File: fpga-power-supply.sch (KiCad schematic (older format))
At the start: 100 parts, among them U14 XC7A100T-FGG484

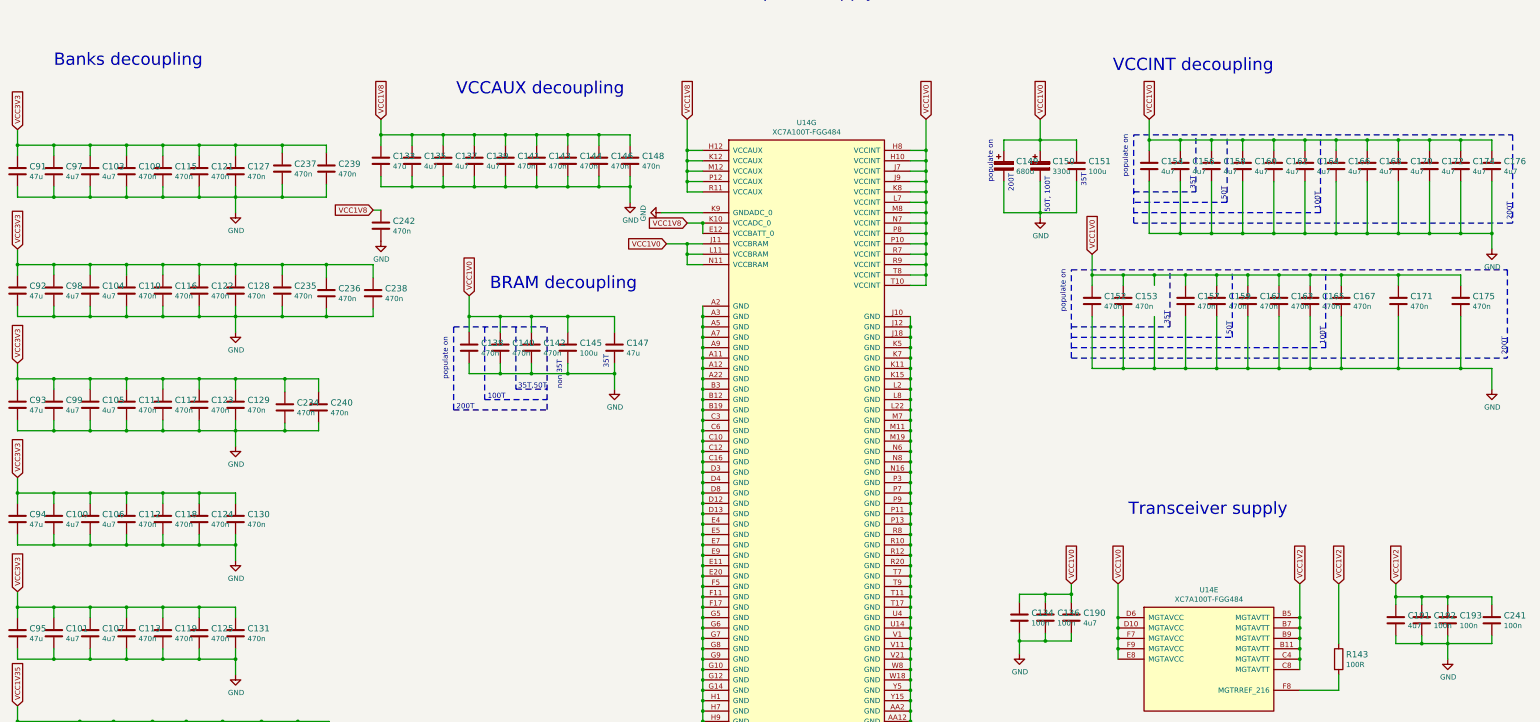
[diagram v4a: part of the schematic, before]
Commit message: Update layout around filtering caps
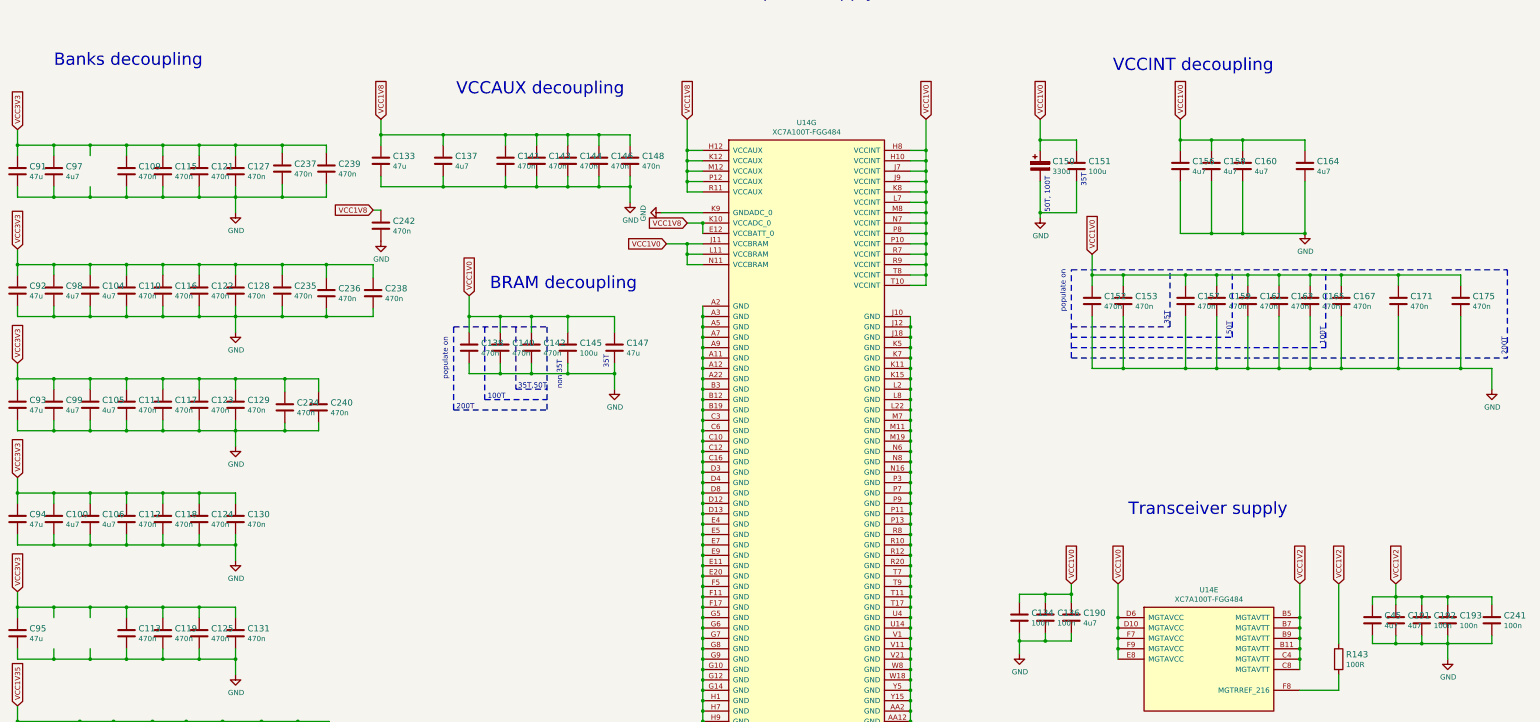
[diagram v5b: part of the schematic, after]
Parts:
- removed C101, C103, C107, C135, C139, C154, C162, C166, C168, C170, C172, C174, C176: C_4u7_0603, artix-dc-scm-footprints:0603-cap, symbol artix-dc-scm:C_4u7_0603
- removed C149: C_680u_KEMET_D, artix-dc-scm-footprints:KEMET_D, symbol artix-dc-scm:C_680u_KEMET_D
- added C45: C_4u7_0603, artix-dc-scm-footprints:0603-cap, symbol artix-dc-scm:C_4u7_0603
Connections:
- net GND: now also C45.2
- net VCC1V2: now also C45.1

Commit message: Generated local libs
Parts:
- C138, C142, C146, C152, C153, C157, C159, C161, C163, C165, C171, C175, C242: footprint antmicro-footprints:0201-res -> artix-dc-scm-footprints:0201-res; symbol antmicroCapacitorsmisc:C_470n_0201 -> artix-dc-scm:C_470n_0201
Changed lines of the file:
@@
 $EndComp
 $Comp
-L antmicroCapacitorsmisc:C_470n_0201 C152
+L artix-dc-scm:C_470n_0201 C152
 U 1 1 603575F3
 P 11500 4350
+AR Path="/603575F3" Ref="C152"  Part="1"
+AR Path="/5FD86C51/603575F3" Ref="C152"  Part="1"
 F 0 "C152" H 11615 4395 60  0000 L CNN
 F 1 "C_470n_0402" H 11500 4200 60  0001 C CNN
-F 2 "antmicro-footprints:0201-res" H 11700 4550 60  0001 L CNN
+F 2 "artix-dc-scm-footprints:0201-res" H 11700 4550 60  0001 L CNN
 F 3 "" H 11500 4350 50  0001 C CNN
 F 4 "TDK" H 11700 4750 60  0001 L CNN "Manufacturer"
@@
 $EndComp
 $Comp
-L antmicroCapacitorsmisc:C_470n_0201 C153
+L artix-dc-scm:C_470n_0201 C153
 U 1 1 60357C64
 P 11800 4350
+AR Path="/60357C64" Ref="C153"  Part="1"
+AR Path="/5FD86C51/60357C64" Ref="C153"  Part="1"
 F 0 "C153" H 11915 4395 60  0000 L CNN
 F 1 "C_470n_0402" H 11800 4200 60  0001 C CNN
-F 2 "antmicro-footprints:0201-res" H 12000 4550 60  0001 L CNN
+F 2 "artix-dc-scm-footprints:0201-res" H 12000 4550 60  0001 L CNN
 F 3 "" H 11800 4350 50  0001 C CNN
 F 4 "TDK" H 12000 4750 60  0001 L CNN "Manufacturer"
@@
 $EndComp
 $Comp
-L antmicroCapacitorsmisc:C_470n_0201 C157
+L artix-dc-scm:C_470n_0201 C157
 U 1 1 603583CC
 P 12400 4350
+AR Path="/603583CC" Ref="C157"  Part="1"
+AR Path="/5FD86C51/603583CC" Ref="C157"  Part="1"
 F 0 "C157" H 12515 4395 60  0000 L CNN
 F 1 "C_470n_0402" H 12400 4200 60  0001 C CNN
-F 2 "antmicro-footprints:0201-res" H 12600 4550 60  0001 L CNN
+F 2 "artix-dc-scm-footprints:0201-res" H 12600 4550 60  0001 L CNN
 F 3 "" H 12400 4350 50  0001 C CNN
 F 4 "TDK" H 12600 4750 60  0001 L CNN "Manufacturer"
@@
 $EndComp
 $Comp
-L antmicroCapacitorsmisc:C_470n_0201 C159
+L artix-dc-scm:C_470n_0201 C159
 U 1 1 6035880F
 P 12700 4350
+AR Path="/6035880F" Ref="C159"  Part="1"
+AR Path="/5FD86C51/6035880F" Ref="C159"  Part="1"
 F 0 "C159" H 12815 4395 60  0000 L CNN
 F 1 "C_470n_0402" H 12700 4200 60  0001 C CNN
-F 2 "antmicro-footprints:0201-res" H 12900 4550 60  0001 L CNN
+F 2 "artix-dc-scm-footprints:0201-res" H 12900 4550 60  0001 L CNN
 F 3 "" H 12700 4350 50  0001 C CNN
 F 4 "TDK" H 12900 4750 60  0001 L CNN "Manufacturer"
@@
 $EndComp
 $Comp
-L antmicroCapacitorsmisc:C_470n_0201 C161
+L artix-dc-scm:C_470n_0201 C161
 U 1 1 60358B3A
 P 13000 4350
+AR Path="/60358B3A" Ref="C161"  Part="1"
+AR Path="/5FD86C51/60358B3A" Ref="C161"  Part="1"
 F 0 "C161" H 13115 4395 60  0000 L CNN
 F 1 "C_470n_0402" H 13000 4200 60  0001 C CNN
-F 2 "antmicro-footprints:0201-res" H 13200 4550 60  0001 L CNN
+F 2 "artix-dc-scm-footprints:0201-res" H 13200 4550 60  0001 L CNN
 F 3 "" H 13000 4350 50  0001 C CNN
 F 4 "TDK" H 13200 4750 60  0001 L CNN "Manufacturer"
@@
 $EndComp
 $Comp
-L antmicroCapacitorsmisc:C_470n_0201 C163
+L artix-dc-scm:C_470n_0201 C163
 U 1 1 60358ED9
 P 13300 4350
+AR Path="/60358ED9" Ref="C163"  Part="1"
+AR Path="/5FD86C51/60358ED9" Ref="C163"  Part="1"
 F 0 "C163" H 13415 4395 60  0000 L CNN
 F 1 "C_470n_0402" H 13300 4200 60  0001 C CNN
-F 2 "antmicro-footprints:0201-res" H 13500 4550 60  0001 L CNN
+F 2 "artix-dc-scm-footprints:0201-res" H 13500 4550 60  0001 L CNN
 F 3 "" H 13300 4350 50  0001 C CNN
 F 4 "TDK" H 13500 4750 60  0001 L CNN "Manufacturer"
@@
 $EndComp
 $Comp
-L antmicroCapacitorsmisc:C_470n_0201 C165
+L artix-dc-scm:C_470n_0201 C165
 U 1 1 60359FF4
 P 13600 4350
+AR Path="/60359FF4" Ref="C165"  Part="1"
+AR Path="/5FD86C51/60359FF4" Ref="C165"  Part="1"
 F 0 "C165" H 13715 4395 60  0000 L CNN
 F 1 "C_470n_0402" H 13600 4200 60  0001 C CNN
-F 2 "antmicro-footprints:0201-res" H 13800 4550 60  0001 L CNN
+F 2 "artix-dc-scm-footprints:0201-res" H 13800 4550 60  0001 L CNN
 F 3 "" H 13600 4350 50  0001 C CNN
 F 4 "TDK" H 13800 4750 60  0001 L CNN "Manufacturer"
@@
 $EndComp
 $Comp
-L antmicroCapacitorsmisc:C_470n_0201 C171
+L artix-dc-scm:C_470n_0201 C171
 U 1 1 6035AD1D
 P 14450 4350
+AR Path="/6035AD1D" Ref="C171"  Part="1"
+AR Path="/5FD86C51/6035AD1D" Ref="C171"  Part="1"
 F 0 "C171" H 14565 4395 60  0000 L CNN
 F 1 "C_470n_0402" H 14450 4200 60  0001 C CNN
-F 2 "antmicro-footprints:0201-res" H 14650 4550 60  0001 L CNN
+F 2 "artix-dc-scm-footprints:0201-res" H 14650 4550 60  0001 L CNN
 F 3 "" H 14450 4350 50  0001 C CNN
 F 4 "TDK" H 14650 4750 60  0001 L CNN "Manufacturer"
@@
 $EndComp
 $Comp
-L antmicroCapacitorsmisc:C_470n_0201 C175
+L artix-dc-scm:C_470n_0201 C175
 U 1 1 6035C6A9
 P 15050 4350
+AR Path="/6035C6A9" Ref="C175"  Part="1"
+AR Path="/5FD86C51/6035C6A9" Ref="C175"  Part="1"
 F 0 "C175" H 15165 4395 60  0000 L CNN
 F 1 "C_470n_0402" H 15050 4200 60  0001 C CNN
-F 2 "antmicro-footprints:0201-res" H 15250 4550 60  0001 L CNN
+F 2 "artix-dc-scm-footprints:0201-res" H 15250 4550 60  0001 L CNN
 F 3 "" H 15050 4350 50  0001 C CNN
 F 4 "TDK" H 15250 4750 60  0001 L CNN "Manufacturer"
@@
 $EndComp
 $Comp
-L antmicroCapacitorsmisc:C_470n_0201 C138
+L artix-dc-scm:C_470n_0201 C138
 U 1 1 603CDFCC
 P 5500 4800
+AR Path="/603CDFCC" Ref="C138"  Part="1"
+AR Path="/5FD86C51/603CDFCC" Ref="C138"  Part="1"
 F 0 "C138" H 5615 4845 60  0000 L CNN
 F 1 "C_470n_0402" H 5500 4650 60  0001 C CNN
-F 2 "antmicro-footprints:0201-res" H 5700 5000 60  0001 L CNN
+F 2 "artix-dc-scm-footprints:0201-res" H 5700 5000 60  0001 L CNN
 F 3 "" H 5500 4800 50  0001 C CNN
 F 4 "TDK" H 5700 5200 60  0001 L CNN "Manufacturer"
@@
 $EndComp
 $Comp
-L antmicroCapacitorsmisc:C_470n_0201 C142
+L artix-dc-scm:C_470n_0201 C142
 U 1 1 603CF11F
 P 6100 4800
+AR Path="/603CF11F" Ref="C142"  Part="1"
+AR Path="/5FD86C51/603CF11F" Ref="C142"  Part="1"
 F 0 "C142" H 6215 4845 60  0000 L CNN
 F 1 "C_470n_0402" H 6100 4650 60  0001 C CNN
-F 2 "antmicro-footprints:0201-res" H 6300 5000 60  0001 L CNN
+F 2 "artix-dc-scm-footprints:0201-res" H 6300 5000 60  0001 L CNN
 F 3 "" H 6100 4800 50  0001 C CNN
 F 4 "TDK" H 6300 5200 60  0001 L CNN "Manufacturer"
@@
 $EndComp
 $Comp
-L antmicroCapacitorsmisc:C_470n_0201 C146
+L artix-dc-scm:C_470n_0201 C146
 U 1 1 6042206F
 P 6750 3000
+AR Path="/6042206F" Ref="C146"  Part="1"
+AR Path="/5FD86C51/6042206F" Ref="C146"  Part="1"
 F 0 "C146" H 6865 3045 60  0000 L CNN
 F 1 "C_470n_0402" H 6750 2850 60  0001 C CNN
-F 2 "antmicro-footprints:0201-res" H 6950 3200 60  0001 L CNN
+F 2 "artix-dc-scm-footprints:0201-res" H 6950 3200 60  0001 L CNN
 F 3 "" H 6750 3000 50  0001 C CNN
 F 4 "TDK" H 6950 3400 60  0001 L CNN "Manufacturer"
@@
 	14925 7200 15350 7200
 $Comp
-L antmicroCapacitorsmisc:C_470n_0201 C242
+L artix-dc-scm:C_470n_0201 C242
 U 1 1 60B881B2
 P 4650 3625
+AR Path="/60B881B2" Ref="C242"  Part="1"
+AR Path="/5FD86C51/60B881B2" Ref="C242"  Part="1"
 F 0 "C242" H 4765 3670 60  0000 L CNN
 F 1 "C_470n_0402" H 4650 3475 60  0001 C CNN
-F 2 "antmicro-footprints:0201-res" H 4850 3825 60  0001 L CNN
+F 2 "artix-dc-scm-footprints:0201-res" H 4850 3825 60  0001 L CNN
 F 3 "" H 4650 3625 50  0001 C CNN
 F 4 "TDK" H 4850 4025 60  0001 L CNN "Manufacturer"

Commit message: Cleaned up schematics
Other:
- moved on the sheet: C109, C115, C121, C127, C133, C137, C141, C143, C144, C146, C148, C164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
